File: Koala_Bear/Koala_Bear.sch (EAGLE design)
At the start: 21 parts

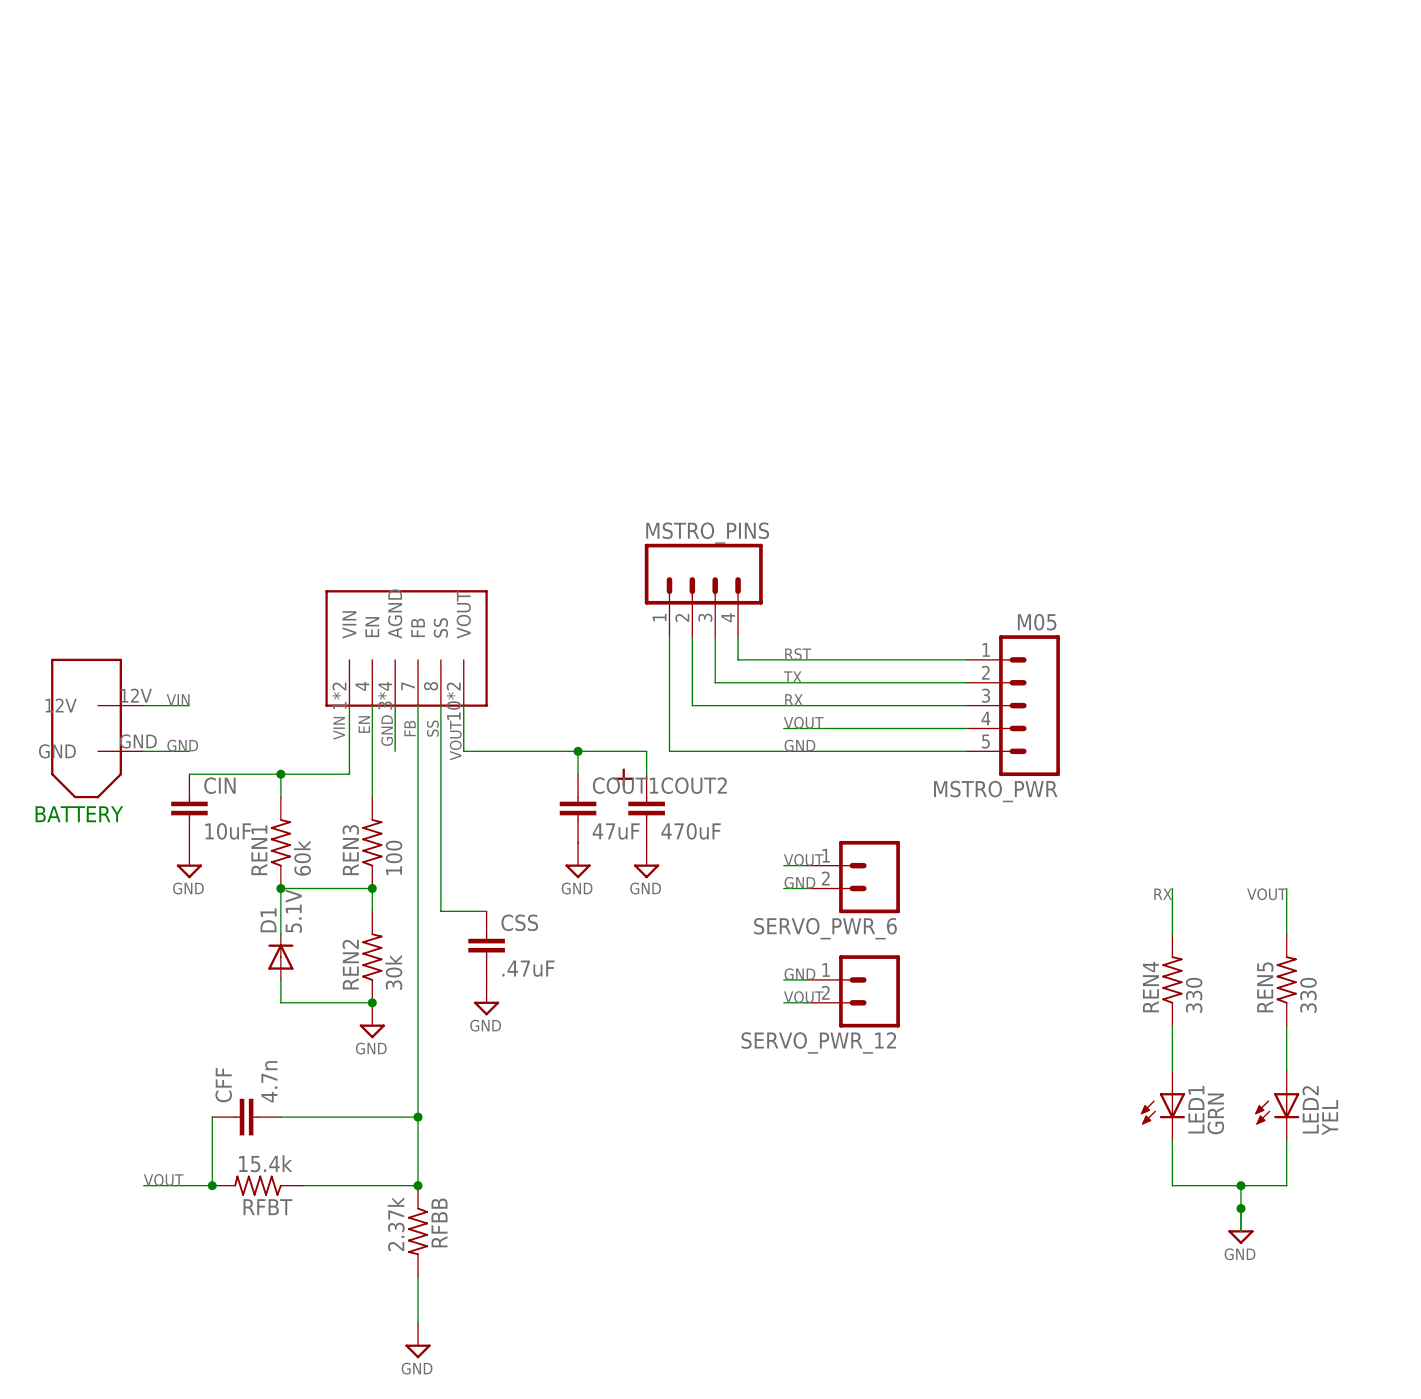
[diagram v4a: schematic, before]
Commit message: Made fixes recommended by Dennis and Yip
Mainly a fix of silkscreen issues with some routing angles also fixed.
Deleted superfluous holes and added a new, useful hole.
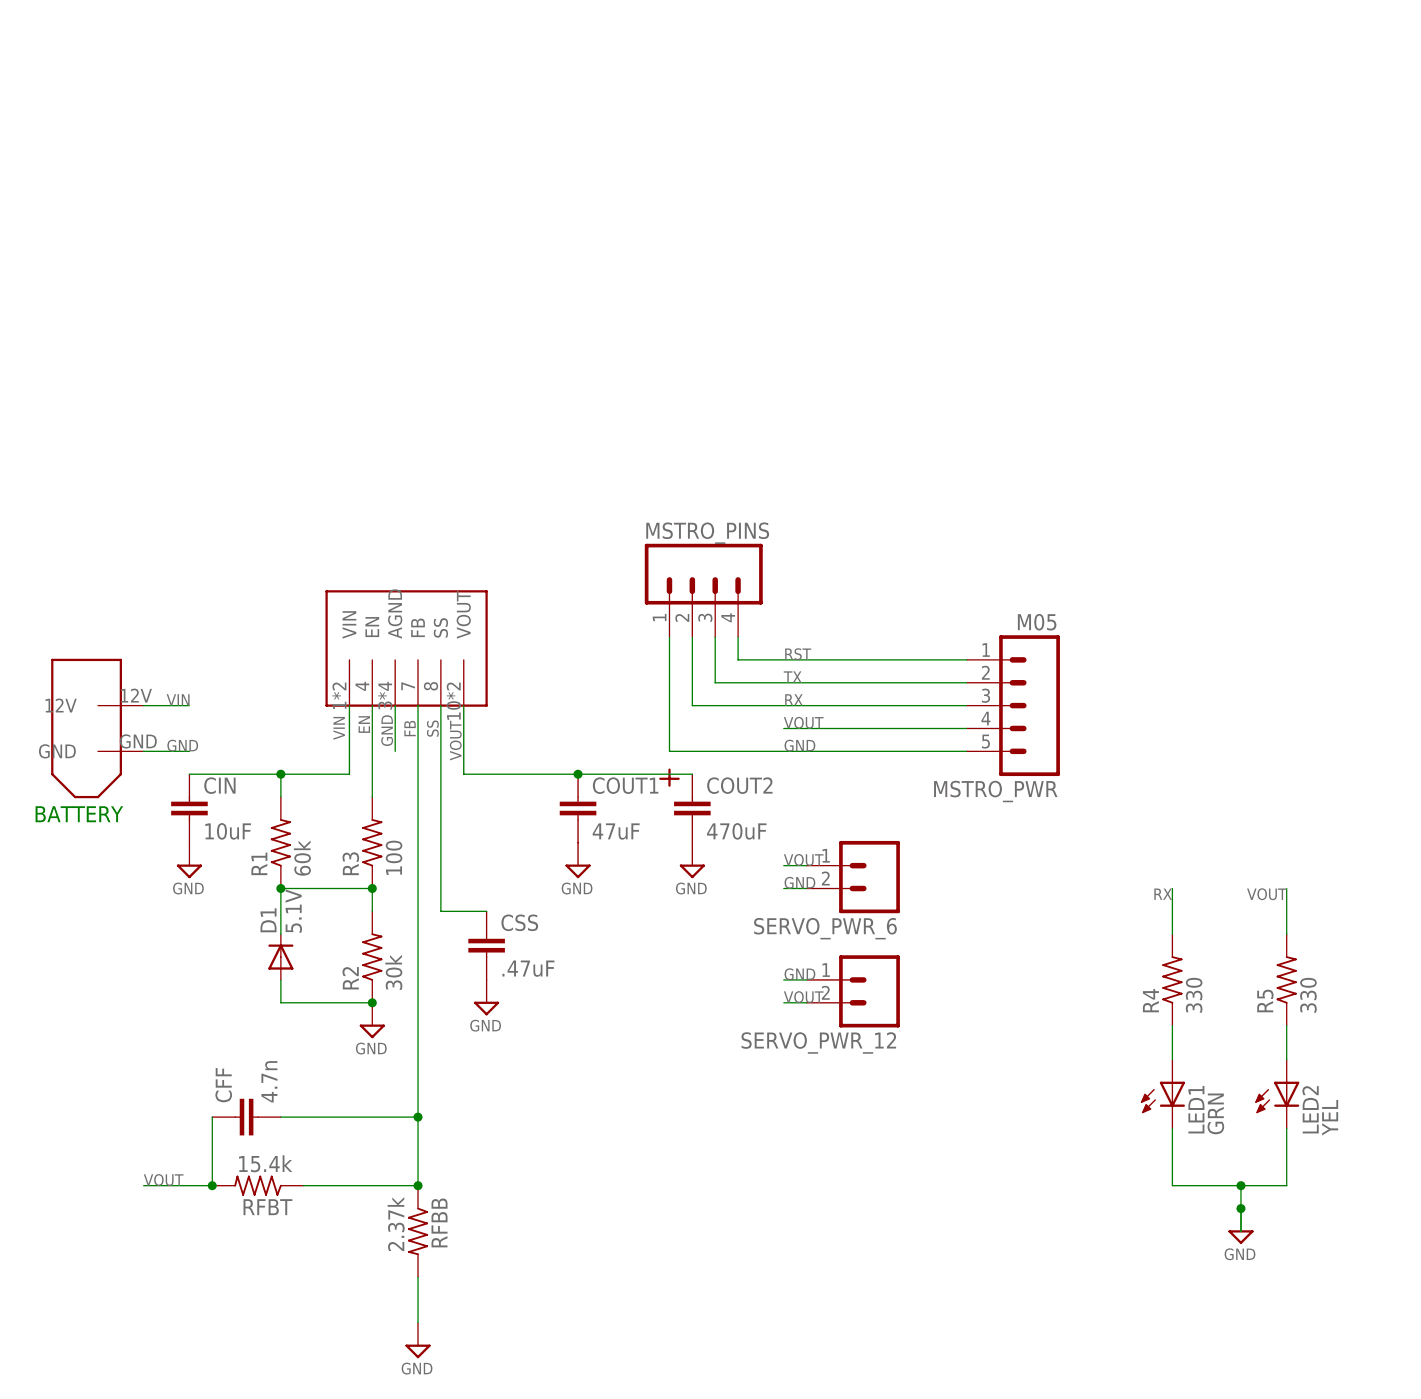
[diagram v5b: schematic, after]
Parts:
- removed REN4, REN5: 330, rcl:R-US_R0603
- added R4, R5: 330, pie:R-US_R0603
- LED1, LED2: device led:LEDCHIP-LED0805 -> pie:LED0805
- renumbered REN1 to R1, REN2 to R2, REN3 to R3
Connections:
- net N$1: now also R4.1; no longer REN4.1
- net N$5: now also R5.1; no longer REN5.1
- net RX: now also R4.2; no longer REN4.2
- net VOUT: now also R5.2; no longer REN5.2
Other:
- moved on the sheet: COUT2, LED1, LED2

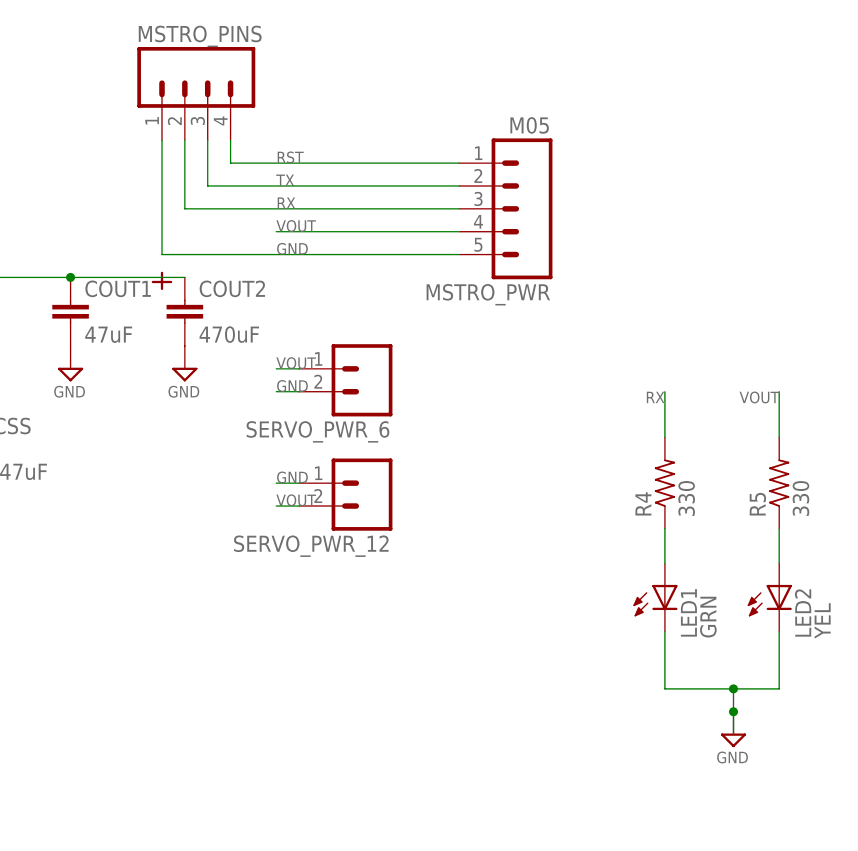
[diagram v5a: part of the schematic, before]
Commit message: Trying to negotiate hole clearances
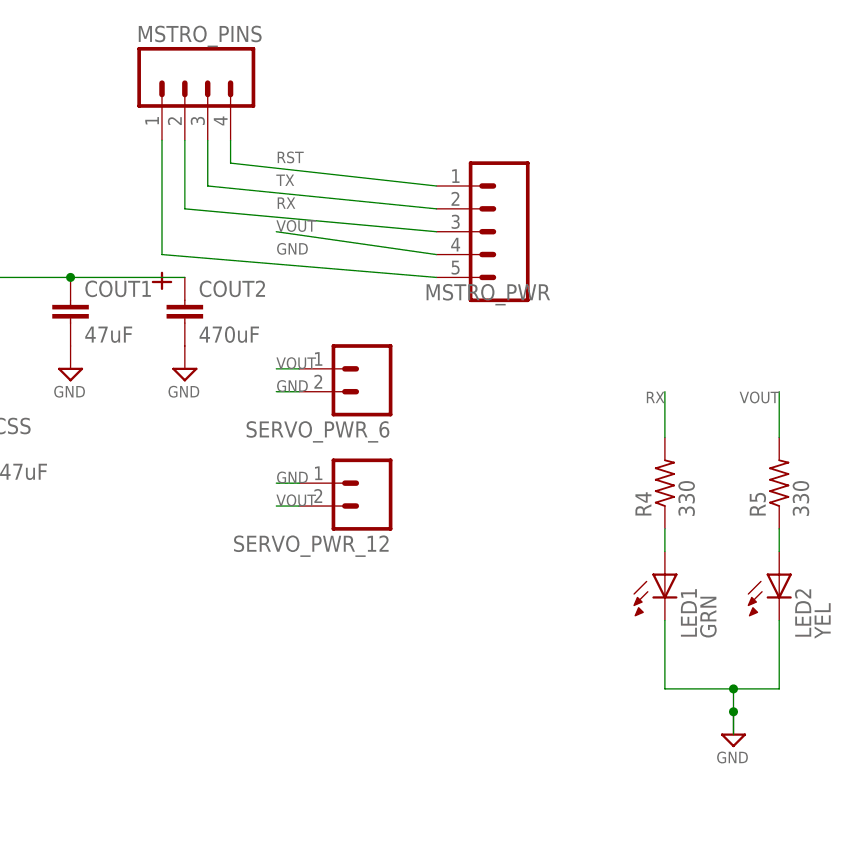
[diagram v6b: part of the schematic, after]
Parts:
- MSTRO_PWR: value M05 -> (none); device pie:M05 -> pie:M05MTA
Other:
- moved on the sheet: LED1, LED2, MSTRO_PWR
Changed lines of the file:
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@@
 <grid distance="0.1" unitdist="inch" unit="inch" style="lines" multiple="1" display="no" altdistance="0.01" altunitdist="inch" altunit="inch"/>
 <layers>
-<layer number="1" name="Top" color="4" fill="1" visible="yes" active="no"/>
-<layer number="16" name="Bottom" color="1" fill="1" visible="yes" active="no"/>
-<layer number="17" name="Pads" color="2" fill="1" visible="yes" active="no"/>
-<layer number="18" name="Vias" color="2" fill="1" visible="yes" active="no"/>
-<layer number="19" name="Unrouted" color="6" fill="1" visible="yes" active="no"/>
-<layer number="20" name="Dimension" color="15" fill="1" visible="yes" active="no"/>
-<layer number="21" name="tPlace" color="7" fill="1" visible="yes" active="no"/>
-<layer number="22" name="bPlace" color="14" fill="1" visible="yes" active="no"/>
-<layer number="23" name="tOrigins" color="15" fill="1" visible="yes" active="no"/>
-<layer number="24" name="bOrigins" color="15" fill="1" visible="yes" active="no"/>
-<layer number="25" name="tNames" color="7" fill="1" visible="yes" active="no"/>
-<layer number="26" name="bNames" color="7" fill="1" visible="yes" active="no"/>
-<layer number="27" name="tValues" color="7" fill="1" visible="yes" active="no"/>
-<layer number="28" name="bValues" color="7" fill="1" visible="yes" active="no"/>
+<layer number="1" name="Top" color="4" fill="1" visible="no" active="no"/>
+<layer number="16" name="Bottom" color="1" fill="1" visible="no" active="no"/>
+<layer number="17" name="Pads" color="2" fill="1" visible="no" active="no"/>
+<layer number="18" name="Vias" color="2" fill="1" visible="no" active="no"/>
+<layer number="19" name="Unrouted" color="6" fill="1" visible="no" active="no"/>
+<layer number="20" name="Dimension" color="15" fill="1" visible="no" active="no"/>
+<layer number="21" name="tPlace" color="7" fill="1" visible="no" active="no"/>
+<layer number="22" name="bPlace" color="14" fill="1" visible="no" active="no"/>
+<layer number="23" name="tOrigins" color="15" fill="1" visible="no" active="no"/>
+<layer number="24" name="bOrigins" color="15" fill="1" visible="no" active="no"/>
+<layer number="25" name="tNames" color="7" fill="1" visible="no" active="no"/>
+<layer number="26" name="bNames" color="7" fill="1" visible="no" active="no"/>
+<layer number="27" name="tValues" color="7" fill="1" visible="no" active="no"/>
+<layer number="28" name="bValues" color="7" fill="1" visible="no" active="no"/>
 <layer number="29" name="tStop" color="7" fill="3" visible="no" active="no"/>
 <layer number="30" name="bStop" color="7" fill="6" visible="no" active="no"/>
@@
 <layer number="35" name="tGlue" color="7" fill="4" visible="no" active="no"/>
 <layer number="36" name="bGlue" color="7" fill="5" visible="no" active="no"/>
-<layer number="37" name="tTest" color="7" fill="1" visible="yes" active="no"/>
-<layer number="38" name="bTest" color="7" fill="1" visible="yes" active="no"/>
+<layer number="37" name="tTest" color="7" fill="1" visible="no" active="no"/>
+<layer number="38" name="bTest" color="7" fill="1" visible="no" active="no"/>
 <layer number="39" name="tKeepout" color="4" fill="11" visible="no" active="no"/>
 <layer number="40" name="bKeepout" color="1" fill="11" visible="no" active="no"/>
@@
 <layer number="44" name="Drills" color="7" fill="1" visible="no" active="no"/>
 <layer number="45" name="Holes" color="7" fill="1" visible="no" active="no"/>
-<layer number="46" name="Milling" color="3" fill="1" visible="yes" active="no"/>
-<layer number="47" name="Measures" color="7" fill="1" visible="yes" active="no"/>
-<layer number="48" name="Document" color="7" fill="1" visible="yes" active="no"/>
-<layer number="49" name="Reference" color="7" fill="1" visible="yes" active="no"/>
-<layer number="50" name="dxf" color="7" fill="1" visible="yes" active="no"/>
-<layer number="51" name="tDocu" color="7" fill="1" visible="yes" active="no"/>
-<layer number="52" name="bDocu" color="7" fill="1" visible="yes" active="no"/>
-<layer number="53" name="tGND_GNDA" color="7" fill="9" visible="yes" active="no"/>
-<layer number="54" name="bGND_GNDA" color="1" fill="9" visible="yes" active="no"/>
-<layer number="56" name="wert" color="7" fill="1" visible="yes" active="no"/>
+<layer number="46" name="Milling" color="3" fill="1" visible="no" active="no"/>
+<layer number="47" name="Measures" color="7" fill="1" visible="no" active="no"/>
+<layer number="48" name="Document" color="7" fill="1" visible="no" active="no"/>
+<layer number="49" name="Reference" color="7" fill="1" visible="no" active="no"/>
+<layer number="50" name="dxf" color="7" fill="1" visible="no" active="no"/>
+<layer number="51" name="tDocu" color="7" fill="1" visible="no" active="no"/>
+<layer number="52" name="bDocu" color="7" fill="1" visible="no" active="no"/>
+<layer number="53" name="tGND_GNDA" color="7" fill="9" visible="no" active="no"/>
+<layer number="54" name="bGND_GNDA" color="1" fill="9" visible="no" active="no"/>
+<layer number="56" name="wert" color="7" fill="1" visible="no" active="no"/>
 <layer number="91" name="Nets" color="2" fill="1" visible="yes" active="yes"/>
 <layer number="92" name="Busses" color="1" fill="1" visible="yes" active="yes"/>
@@
 <part name="MSTRO_PINS" library="pie_new" deviceset="M04" device="1X04-MTA"/>
 <part name="XT60" library="pie_new" deviceset="XT60CONNECTOR" device=""/>
-<part name="MSTRO_PWR" library="pie" deviceset="M05" device=""/>
+<part name="MSTRO_PWR" library="pie" deviceset="M05" device="MTA"/>
 <part name="SERVO_PWR_6" library="pie" deviceset="M02" device="PTH"/>
 <part name="SERVO_PWR_12" library="pie" deviceset="M02" device="PTH"/>
@@
 <pinref part="MSTRO_PINS" gate="G$1" pin="1"/>
 <wire x1="43.18" y1="53.34" x2="43.18" y2="40.64" width="0.1524" layer="91"/>
-<wire x1="43.18" y1="40.64" x2="76.2" y2="40.64" width="0.1524" layer="91"/>
+<wire x1="43.18" y1="40.64" x2="73.66" y2="38.1" width="0.1524" layer="91"/>
 </segment>
 <segment>
@@
 <segment>
 <pinref part="LED1" gate="G$1" pin="C"/>
-<wire x1="99.06" y1="-1.27" x2="99.06" y2="-7.62" width="0.1524" layer="91"/>
+<wire x1="99.06" y1="0" x2="99.06" y2="-7.62" width="0.1524" layer="91"/>
 <pinref part="LED2" gate="G$1" pin="C"/>
 <wire x1="99.06" y1="-7.62" x2="106.68" y2="-7.62" width="0.1524" layer="91"/>
 <wire x1="106.68" y1="-7.62" x2="111.76" y2="-7.62" width="0.1524" layer="91"/>
-<wire x1="111.76" y1="-7.62" x2="111.76" y2="-1.27" width="0.1524" layer="91"/>
+<wire x1="111.76" y1="-7.62" x2="111.76" y2="0" width="0.1524" layer="91"/>
 <junction x="106.68" y="-7.62"/>
 <wire x1="106.68" y1="-7.62" x2="106.68" y2="-10.16" width="0.1524" layer="91"/>
@@
 <segment>
 <pinref part="MSTRO_PWR" gate="G$1" pin="4"/>
-<wire x1="76.2" y1="43.18" x2="55.88" y2="43.18" width="0.1524" layer="91"/>
+<wire x1="73.66" y1="40.64" x2="55.88" y2="43.18" width="0.1524" layer="91"/>
 <label x="55.88" y="43.18" size="1.27" layer="95" font="vector"/>
 </segment>
@@
 <wire x1="45.72" y1="53.34" x2="45.72" y2="45.72" width="0.1524" layer="91"/>
 <pinref part="MSTRO_PWR" gate="G$1" pin="3"/>
-<wire x1="45.72" y1="45.72" x2="76.2" y2="45.72" width="0.1524" layer="91"/>
+<wire x1="45.72" y1="45.72" x2="73.66" y2="43.18" width="0.1524" layer="91"/>
 <label x="55.88" y="45.72" size="1.27" layer="95"/>
 </segment>
@@
 <wire x1="48.26" y1="53.34" x2="48.26" y2="48.26" width="0.1524" layer="91"/>
 <pinref part="MSTRO_PWR" gate="G$1" pin="2"/>
-<wire x1="48.26" y1="48.26" x2="76.2" y2="48.26" width="0.1524" layer="91"/>
+<wire x1="48.26" y1="48.26" x2="73.66" y2="45.72" width="0.1524" layer="91"/>
 <label x="55.88" y="48.26" size="1.27" layer="95"/>
 </segment>
@@
 <wire x1="50.8" y1="53.34" x2="50.8" y2="50.8" width="0.1524" layer="91"/>
 <pinref part="MSTRO_PWR" gate="G$1" pin="1"/>
-<wire x1="50.8" y1="50.8" x2="76.2" y2="50.8" width="0.1524" layer="91"/>
+<wire x1="50.8" y1="50.8" x2="73.66" y2="48.26" width="0.1524" layer="91"/>
 <label x="55.88" y="50.8" size="1.27" layer="95"/>
 </segment>
@@
 <segment>
 <pinref part="R4" gate="G$1" pin="1"/>
-<wire x1="99.06" y1="10.16" x2="99.06" y2="6.35" width="0.1524" layer="91"/>
+<wire x1="99.06" y1="10.16" x2="99.06" y2="7.62" width="0.1524" layer="91"/>
 <pinref part="LED1" gate="G$1" pin="A"/>
 </segment>
@@
 <segment>
 <pinref part="R5" gate="G$1" pin="1"/>
-<wire x1="111.76" y1="10.16" x2="111.76" y2="6.35" width="0.1524" layer="91"/>
+<wire x1="111.76" y1="10.16" x2="111.76" y2="7.62" width="0.1524" layer="91"/>
 <pinref part="LED2" gate="G$1" pin="A"/>
 </segment>
